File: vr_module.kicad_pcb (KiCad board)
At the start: 4 copper layers, 16.9 x 22.6 mm, 26 parts, among them J1 Conn_01x07, U1 LM393, U2 NC7SB3157P6X, U3 74HC00, U4 NC7SB3157P6X, U5 SRV05-4, U6 MCP6004

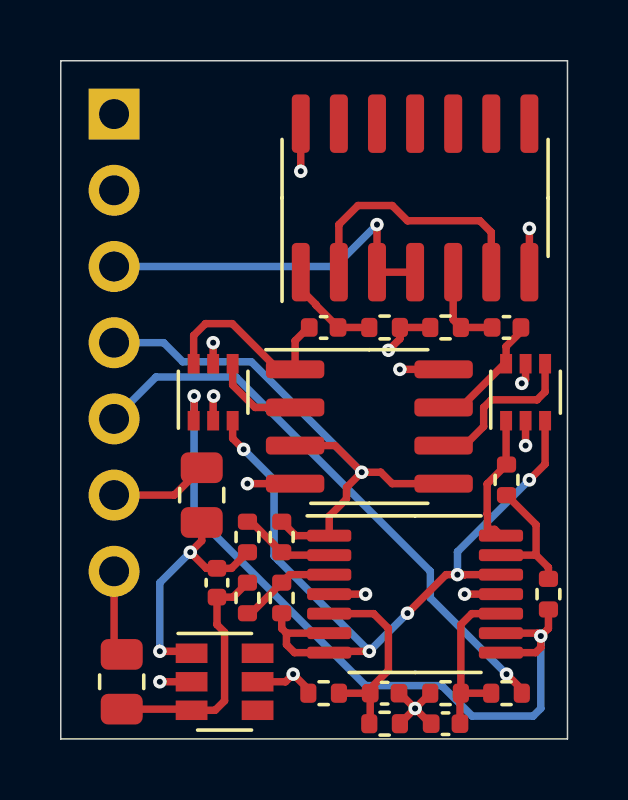
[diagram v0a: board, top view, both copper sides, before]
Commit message: add power caps, silk on bottom
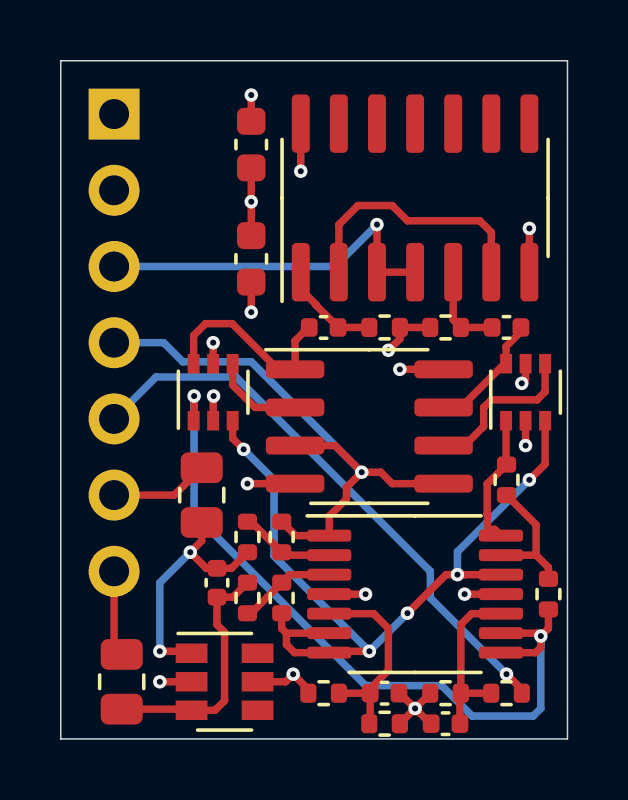
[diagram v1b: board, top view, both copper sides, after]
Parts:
- added C6: 10n, Capacitor_SMD:C_0603_1608Metric, F.Cu at (64.6, 81.0)
- added C7: 1u, Capacitor_SMD:C_0603_1608Metric, F.Cu at (64.6, 84.8)
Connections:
- U5 pad 4: Net-(U5-Pad4) -> (no net)
- U5 pad 6: Net-(U5-Pad6) -> (no net)
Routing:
- net +5V: track 7.80 -> 10.1 mm, vias 6 -> 7
- net GND: track 11.8 -> 13.7 mm, vias 8 -> 10
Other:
- board text added: "5V"
- board text added: "Analog out"
- board text added: "GND"
- board text added: "Output"
- board text added: "Threshold input"
- board text added: "VR+"
- board text added: "VR-"

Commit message: filter pwm harder
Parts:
- added C8: 470n, Capacitor_SMD:C_0402_1005Metric, F.Cu at (72.9, 100.3)
- added R15: 10k, Resistor_SMD:R_0402_1005Metric, F.Cu at (74.5, 99.1)
- R12: value 33k -> 68k
- moved R10 2.03 mm to (67.1, 100.3), turned to 180 degrees
- moved C3 0.56 mm to (70.6, 100.3)
- moved R11 0.30 mm to (72.8, 99.3)
- moved R12 0.20 mm to (70.9, 99.3)
- moved C4 0.10 mm to (69.0, 99.3)
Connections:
- R11 pad 1: thresh_input -> Net-(C8-Pad1)
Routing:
- net Net-(C8-Pad1): track 0.00 -> 2.32 mm
- net GND: track 13.7 -> 15.0 mm, vias 10 -> 12
- net thresh_low: track 25.8 -> 24.6 mm
- net thresh_input: track 19.1 -> 19.7 mm
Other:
- net class Default: clearance 0.2 -> 0.1524
- rule trace_clearance: 0.2 -> 0.1524
- rule trace_min: 0.2 -> 0.1524

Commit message: s
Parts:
- moved C5 0.27 mm to (63.7, 95.5)
- moved R4 0.24 mm to (64.7, 96.0)
- moved R3 0.20 mm to (64.7, 94.1)
- moved R5 0.15 mm to (65.7, 96.0)
- moved R6 0.08 mm to (65.7, 94.1)
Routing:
- net Net-(C5-Pad1): track 8.31 -> 7.33 mm, vias 2 -> 0
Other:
- rule pad_to_mask_clearance: 0 -> 0.049

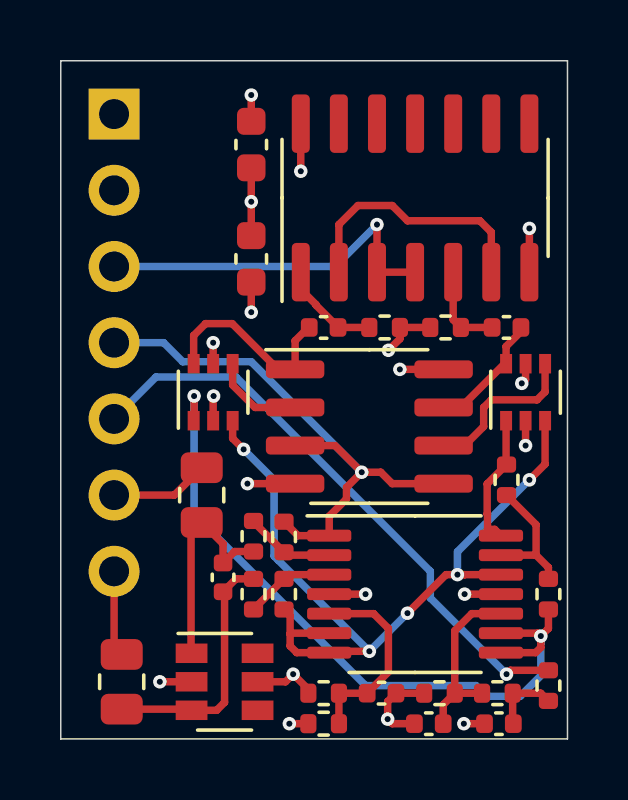
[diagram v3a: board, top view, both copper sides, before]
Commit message: add filter caps
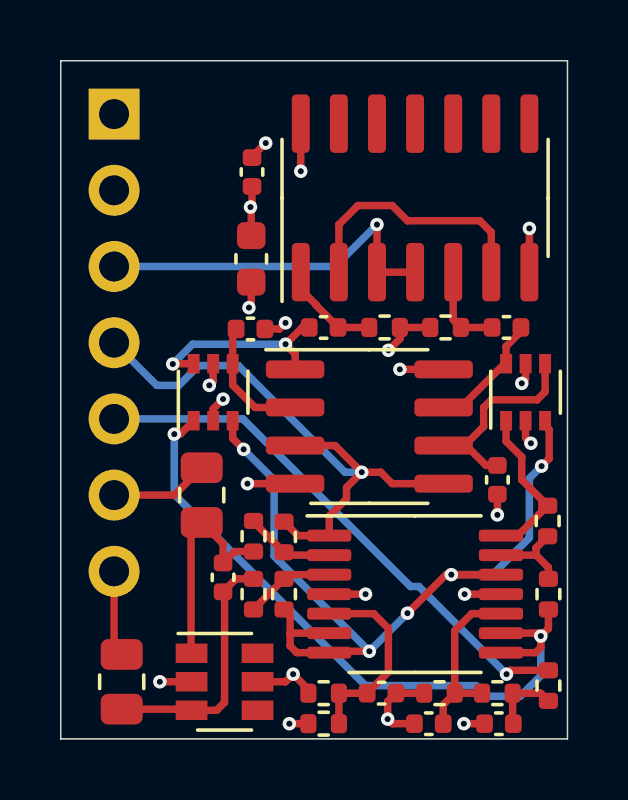
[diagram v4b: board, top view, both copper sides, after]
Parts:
- added C10: 10n, Capacitor_SMD:C_0402_1005Metric, F.Cu at (72.8, 92.2)
- added C9: 10n, Capacitor_SMD:C_0402_1005Metric, F.Cu at (64.6, 87.2)
- C6: footprint Capacitor_SMD:C_0603_1608Metric -> Capacitor_SMD:C_0402_1005Metric
- R15: value 10k -> 12k
- moved R14 1.94 mm to (74.5, 93.6)
- moved C6 0.91 mm to (64.7, 81.9)
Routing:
- net Net-(C10-Pad2): track 5.43 -> 7.50 mm
- net thresh_input: track 19.7 -> 18.1 mm
- net Net-(R13-Pad1): track 4.54 -> 2.92 mm
- net Net-(C9-Pad2): track 3.10 -> 4.31 mm
- net GND: track 15.0 -> 16.1 mm, vias 12 -> 14
- net Vref: track 26.7 -> 27.7 mm
- net thresh_low: track 24.6 -> 23.6 mm
- net thresh_high: track 4.44 -> 5.38 mm
- net analog_out: track 19.8 -> 20.3 mm
- net +5V: track 10.1 -> 9.55 mm
- net Net-(C1-Pad2): track 6.73 -> 6.72 mm, vias 0 -> 2
